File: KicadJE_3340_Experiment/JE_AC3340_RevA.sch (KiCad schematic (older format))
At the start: 64 parts

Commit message: Update JE_AC3340_RevA.sch
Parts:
- added C?: 10n, Capacitor_SMD:C_0805_2012Metric_Pad1.15x1.40mm_HandSolder, symbol Device:C
- added C?: 1n alt, Capacitor_SMD:C_0805_2012Metric_Pad1.15x1.40mm_HandSolder, symbol Device:C
- added C?: 1n poly, Capacitor_THT:C_Rect_L7.0mm_W2.0mm_P5.00mm, symbol Device:C
- added C? (x2): 100n, Capacitor_SMD:C_0805_2012Metric_Pad1.15x1.40mm_HandSolder, symbol Device:C
- added C?: 220p, Capacitor_SMD:C_0805_2012Metric_Pad1.15x1.40mm_HandSolder, symbol Device:C
- added D?: 1N4148, Diode_SMD:D_SOD-123, symbol Device:D
- added D?: Germanium, symbol Device:D
- added JP?: Jumper_3_Bridged12, Jumper:SolderJumper-3_P1.3mm_Bridged12_Pad1.0x1.5mm_NumberLabels, symbol Jumper:Jumper_3_Bridged12
- added Q?: MMBT3906, Package_TO_SOT_SMD:SOT-23, symbol Transistor_BJT:MMBT3906
- added R? (x4): 100k, Resistor_SMD:R_0805_2012Metric_Pad1.15x1.40mm_HandSolder, symbol Device:R
- added R?: 10k, Resistor_SMD:R_0805_2012Metric_Pad1.15x1.40mm_HandSolder, symbol Device:R
- added R?: 20k, Resistor_SMD:R_0805_2012Metric_Pad1.15x1.40mm_HandSolder, symbol Device:R
- added R?: 1k82, Resistor_SMD:R_0805_2012Metric_Pad1.15x1.40mm_HandSolder, symbol Device:R
- added R?: 6k04, Resistor_SMD:R_0805_2012Metric_Pad1.15x1.40mm_HandSolder, symbol Device:R
- added R?: 26k7, Resistor_SMD:R_0805_2012Metric_Pad1.15x1.40mm_HandSolder, symbol Device:R
- added R?: 1M2, Resistor_SMD:R_0805_2012Metric_Pad1.15x1.40mm_HandSolder, symbol Device:R
- added R? (x2): 47k, Resistor_SMD:R_0805_2012Metric_Pad1.15x1.40mm_HandSolder, symbol Device:R
- added RV?: 5k, Potentiometer_THT:Potentiometer_Bourns_3296W_Vertical, symbol Device:R_POT_TRIM
- added U?: TL072, AJ-Dropbox-Kicad:AJ_SO-8_5.3x6.2mm_P1.27mm, symbol Amplifier_Operational:TL072
- added U?: AS3340, symbol Audio:AS3340
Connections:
- net +12L: no longer U?.16 (VCC)
- net +12VA: now also U?.16 (VCC), U?.16 (VCC)
- net +5V: now also JP?.1 (A)
- net -12VA: now also R?.2
- net -5V: now also R?.2, R?.2, RV?.1, RV?.2, U?.3 (VEE)
- net CVIn1: now also U?.15 (VFCI)
- net FM_Lin_In4: now also U?.13 (VLFI)
- net GND: now also C?.1, C?.1, C?.1, C?.2, R?.1, R?.1, U?.12 (GND), U?.3 (+), U?.7 (VHFT)
- net PWM_In5: now also C?.2, D?.1 (K), R?.1, U?.1, U?.5 (VPWM); no longer D?.1 (K), D?.2 (A), R?.1
- net SoftSyncIn2: now also C?.2
- net VP_2: now also R?.2, U?.4 (VP)
- net VSO_3: now also Q?.2 (E), U?.8 (VSO)
- net VTO_1: now also U?.10 (VTO)
- net Vee: no longer R?.2, RV?.1, RV?.2
- new net: D?.1 (K), D?.2 (A), R?.1, R?.2
- new net: R?.2, RV?.1, RV?.2
- new net: C?.1, D?.2 (A), R?.1, R?.1, R?.1, R?.2, U?.2 (-)
- new net: R?.1, R?.2
- new net: R?.1, U?.1 (SCALE1)
- new net: C?.1, C?.2, U?.11 (CAP)
- new net: R?.2, U?.14 (VS)
- new net: R?.1, R?.1, U?.2 (SCALE2)
- new net: C?.2, JP?.3 (B), U?.9 (VSSI)
- new net: R?.2, RV?.3
- new net: D?.1 (K), Q?.1 (B), R?.1, R?.1
- new net: C?.2, D?.2 (A), Q?.3 (C)
- new net: C?.1, R?.2
- new net: JP?.2 (C), R?.2
- new net poly: R?.2
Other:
- note added: "1n timing cap\n0805 as backup\nTHT 1000 pf poly"
- note added: "Prophet 5"
- note added: "Prophet T8"

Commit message: Octave switch JE
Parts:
- added R?: 82k, Resistor_SMD:R_0805_2012Metric_Pad1.15x1.40mm_HandSolder, symbol Device:R
- added R?: 20k, Resistor_SMD:R_0805_2012Metric_Pad1.15x1.40mm_HandSolder, symbol Device:R
- added R?: 47k, Resistor_SMD:R_0805_2012Metric_Pad1.15x1.40mm_HandSolder, symbol Device:R
- added R?: 470R, Resistor_SMD:R_0805_2012Metric_Pad1.15x1.40mm_HandSolder, symbol Device:R
- added SW?: Octave (3 state), AJ-Dropbox-Kicad:SP1MS1, symbol Switch:SW_SPDT
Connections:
- net +5V: now also R?.2, R?.2
- net GND: now also R?.2, SW?.1 (A)
- new net: R?.1, R?.2, SW?.2 (B)
- new net: R?.1, SW?.3 (C)
- new net: R?.1, R?.1
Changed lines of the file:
@@
 AR Path="/5E4B0DD9/5F66CD2B" Ref="U?"  Part="1"
 AR Path="/5E62ACA1/5F66CD2B" Ref="U?"  Part="1"
+AR Path="/5F49A670/5F66CD2B" Ref="U?"  Part="1"
 F 0 "U?" H 10300 4631 50  0000 C CNN
 F 1 "AS3340" H 10300 4540 50  0000 C CNN
@@
 AR Path="/5E4B0DD9/5F66CD3F" Ref="C?"  Part="1"
 AR Path="/5E62ACA1/5F66CD3F" Ref="C?"  Part="1"
+AR Path="/5F49A670/5F66CD3F" Ref="C?"  Part="1"
 F 0 "C?" H 9200 4450 50  0000 L CNN
 F 1 "1n poly" H 9125 4200 50  0000 L CNN
@@
 AR Path="/5E4B0DD9/5F66CD4A" Ref="R?"  Part="1"
 AR Path="/5E62ACA1/5F66CD4A" Ref="R?"  Part="1"
+AR Path="/5F49A670/5F66CD4A" Ref="R?"  Part="1"
 F 0 "R?" V 9550 4450 50  0000 C CNN
 F 1 "1k82" V 9675 4450 50  0000 C CNN
@@
 AR Path="/5E4B0DD9/5F66CD58" Ref="#PWR?"  Part="1"
 AR Path="/5E62ACA1/5F66CD58" Ref="#PWR?"  Part="1"
+AR Path="/5F49A670/5F66CD58" Ref="#PWR?"  Part="1"
 F 0 "#PWR?" H 9425 4400 50  0001 C CNN
 F 1 "GND" H 9430 4477 50  0000 C CNN
@@
 AR Path="/5E4B0DD9/5F66CD63" Ref="R?"  Part="1"
 AR Path="/5E62ACA1/5F66CD63" Ref="R?"  Part="1"
+AR Path="/5F49A670/5F66CD63" Ref="R?"  Part="1"
 F 0 "R?" V 9375 3400 50  0000 C CNN
 F 1 "6k04" V 9425 3250 50  0000 C CNN
@@
 AR Path="/5E4B0DD9/5F66CD69" Ref="R?"  Part="1"
 AR Path="/5E62ACA1/5F66CD69" Ref="R?"  Part="1"
+AR Path="/5F49A670/5F66CD69" Ref="R?"  Part="1"
 F 0 "R?" V 9325 3275 50  0000 C CNN
 F 1 "26k7" V 9425 3150 50  0000 C CNN
@@
 AR Path="/5E4B0DD9/5F66CD6F" Ref="RV?"  Part="1"
 AR Path="/5E62ACA1/5F66CD6F" Ref="RV?"  Part="1"
+AR Path="/5F49A670/5F66CD6F" Ref="RV?"  Part="1"
 F 0 "RV?" V 9150 3050 50  0000 C CNN
 F 1 "5k" V 9025 3175 50  0000 C CNN
@@
 AR Path="/5E4B0DD9/5F66CD7D" Ref="#PWR?"  Part="1"
 AR Path="/5E62ACA1/5F66CD7D" Ref="#PWR?"  Part="1"
+AR Path="/5F49A670/5F66CD7D" Ref="#PWR?"  Part="1"
 F 0 "#PWR?" H 10400 4350 50  0001 C CNN
 F 1 "GND" H 10405 4427 50  0000 C CNN
@@
 AR Path="/5E4B0DD9/5F66CD91" Ref="R?"  Part="1"
 AR Path="/5E62ACA1/5F66CD91" Ref="R?"  Part="1"
+AR Path="/5F49A670/5F66CD91" Ref="R?"  Part="1"
 F 0 "R?" V 9375 3500 50  0000 C CNN
 F 1 "1M2" V 9425 3350 50  0000 C CNN
@@
 U 1 1 5F66CD99
 P 8675 3150
+AR Path="/5E62ACA1/5F66CD99" Ref="#PWR?"  Part="1"
+AR Path="/5F49A670/5F66CD99" Ref="#PWR?"  Part="1"
 F 0 "#PWR?" H 8675 3250 50  0001 C CNN
 F 1 "-5V" H 8690 3323 50  0000 C CNN
@@
 AR Path="/5E4B0DD9/5F66CD9F" Ref="#PWR?"  Part="1"
 AR Path="/5E62ACA1/5F66CD9F" Ref="#PWR?"  Part="1"
+AR Path="/5F49A670/5F66CD9F" Ref="#PWR?"  Part="1"
 F 0 "#PWR?" H 9125 3225 50  0001 C CNN
 F 1 "-12VA" H 9140 3548 50  0000 C CNN
@@
 AR Path="/5F18E4B5/5F66CDA9" Ref="C?"  Part="1"
 AR Path="/5E62ACA1/5F66CDA9" Ref="C?"  Part="1"
+AR Path="/5F49A670/5F66CDA9" Ref="C?"  Part="1"
 F 0 "C?" H 8925 4450 50  0000 L CNN
 F 1 "100n" H 8850 4275 50  0000 L CNN
@@
 U 1 1 5F66CDB6
 P 10300 4625
+AR Path="/5E62ACA1/5F66CDB6" Ref="#PWR?"  Part="1"
+AR Path="/5F49A670/5F66CDB6" Ref="#PWR?"  Part="1"
 F 0 "#PWR?" H 10300 4725 50  0001 C CNN
 F 1 "-5V" H 10315 4798 50  0000 C CNN
@@
 U 1 1 5F66CDBC
 P 8550 3950
+AR Path="/5E62ACA1/5F66CDBC" Ref="Q?"  Part="1"
+AR Path="/5F49A670/5F66CDBC" Ref="Q?"  Part="1"
 F 0 "Q?" H 8741 3904 50  0000 L CNN
 F 1 "MMBT3906" H 8741 3995 50  0000 L CNN
@@
 AR Path="/5E4B0DD9/5F66CDC3" Ref="C?"  Part="1"
 AR Path="/5E62ACA1/5F66CDC3" Ref="C?"  Part="1"
+AR Path="/5F49A670/5F66CDC3" Ref="C?"  Part="1"
 F 0 "C?" V 7550 4150 50  0000 L CNN
 F 1 "220p" V 7650 4150 50  0000 L CNN
@@
 AR Path="/5E4B0DD9/5F66CDC9" Ref="R?"  Part="1"
 AR Path="/5E62ACA1/5F66CDC9" Ref="R?"  Part="1"
+AR Path="/5F49A670/5F66CDC9" Ref="R?"  Part="1"
 F 0 "R?" V 7900 4025 50  0000 C CNN
 F 1 "47k" V 8000 4100 50  0000 C CNN
@@
 AR Path="/5E4B0DD9/5F66CDD1" Ref="R?"  Part="1"
 AR Path="/5E62ACA1/5F66CDD1" Ref="R?"  Part="1"
+AR Path="/5F49A670/5F66CDD1" Ref="R?"  Part="1"
 F 0 "R?" V 8125 3725 50  0000 C CNN
 F 1 "47k" V 8225 3800 50  0000 C CNN
@@
 U 1 1 5F66CDDA
 P 7975 3400
+AR Path="/5E62ACA1/5F66CDDA" Ref="#PWR?"  Part="1"
+AR Path="/5F49A670/5F66CDDA" Ref="#PWR?"  Part="1"
 F 0 "#PWR?" H 7975 3250 50  0001 C CNN
 F 1 "+5V" H 7990 3573 50  0000 C CNN
@@
 AR Path="/5F18E4B5/5F66CDE3" Ref="C?"  Part="1"
 AR Path="/5E62ACA1/5F66CDE3" Ref="C?"  Part="1"
+AR Path="/5F49A670/5F66CDE3" Ref="C?"  Part="1"
 F 0 "C?" H 8650 4450 50  0000 L CNN
 F 1 "100n" H 8550 4275 50  0000 L CNN
@@
 U 1 1 5F66CDEE
 P 8425 4175
+AR Path="/5E62ACA1/5F66CDEE" Ref="D?"  Part="1"
+AR Path="/5F49A670/5F66CDEE" Ref="D?"  Part="1"
 F 0 "D?" H 8325 4250 50  0000 C CNN
 F 1 "Germanium" H 8325 4100 50  0000 C CNN
@@
 U 1 1 5F66CDFA
 P 8225 3450
+AR Path="/5E62ACA1/5F66CDFA" Ref="JP?"  Part="1"
+AR Path="/5F49A670/5F66CDFA" Ref="JP?"  Part="1"
 F 0 "JP?" H 8225 3654 50  0000 C CNN
 F 1 "Jumper_3_Bridged12" H 8225 3563 50  0000 C CNN
@@
 	1    0    0    -1
 $EndComp
+$Comp
+L Switch:SW_SPDT SW?
+U 1 1 5F6B865F
+P 1700 5675
+AR Path="/5F6B865F" Ref="SW?"  Part="1"
+AR Path="/5C8C5FC0/5F6B865F" Ref="SW?"  Part="1"
+AR Path="/5CAAE8D3/5F6B865F" Ref="SW?"  Part="1"
+AR Path="/5E4B0DD9/5F6B865F" Ref="SW?"  Part="1"
+AR Path="/5E62ACA1/5F6B865F" Ref="SW?"  Part="1"
+AR Path="/5F49A670/5F6B865F" Ref="SW?"  Part="1"
+F 0 "SW?" H 2100 5700 50  0000 C CNN
+F 1 "Octave (3 state)" H 1750 5475 50  0000 C CNN
+F 2 "AJ-Dropbox-Kicad:SP1MS1" H 1700 5675 50  0001 C CNN
+F 3 "~" H 1700 5675 50  0001 C CNN
+	1    1700 5675
+	-1   0    0    1
+$EndComp
+$Comp
+L Envelope-cache-2018-08-04-13-00-04:+5V #PWR?
+U 1 1 5F6F74CC
+P 1500 5300
+AR Path="/5E62ACA1/5F6F74CC" Ref="#PWR?"  Part="1"
+AR Path="/5F49A670/5F6F74CC" Ref="#PWR?"  Part="1"
+F 0 "#PWR?" H 1500 5150 50  0001 C CNN
+F 1 "+5V" H 1515 5473 50  0000 C CNN
+F 2 "" H 1500 5300 50  0001 C CNN
+F 3 "" H 1500 5300 50  0001 C CNN
+	1    1500 5300
+	1    0    0    -1
+$EndComp
+$Comp
+L Device:R R?
+U 1 1 5F6F7A40
+P 2025 5500
+AR Path="/5F6F7A40" Ref="R?"  Part="1"
+AR Path="/5C8C5FC0/5F6F7A40" Ref="R?"  Part="1"
+AR Path="/5CAAE8D3/5F6F7A40" Ref="R?"  Part="1"
+AR Path="/5E4B0DD9/5F6F7A40" Ref="R?"  Part="1"
+AR Path="/5E62ACA1/5F6F7A40" Ref="R?"  Part="1"
+AR Path="/5F49A670/5F6F7A40" Ref="R?"  Part="1"
+F 0 "R?" V 1950 5425 50  0000 C CNN
+F 1 "82k" V 2025 5500 50  0000 C CNN
+F 2 "Resistor_SMD:R_0805_2012Metric_Pad1.15x1.40mm_HandSolder" V 1955 5500 50  0001 C CNN
+F 3 "~" H 2025 5500 50  0001 C CNN
+	1    2025 5500
+	-1   0    0    1
+$EndComp
+$Comp
+L Device:R R?
+U 1 1 5F6F8705
+P 2025 5850
+AR Path="/5F6F8705" Ref="R?"  Part="1"
+AR Path="/5C8C5FC0/5F6F8705" Ref="R?"  Part="1"
+AR Path="/5CAAE8D3/5F6F8705" Ref="R?"  Part="1"
+AR Path="/5E4B0DD9/5F6F8705" Ref="R?"  Part="1"
+AR Path="/5E62ACA1/5F6F8705" Ref="R?"  Part="1"
+AR Path="/5F49A670/5F6F8705" Ref="R?"  Part="1"
+F 0 "R?" V 1950 5775 50  0000 C CNN
+F 1 "20k" V 2025 5850 50  0000 C CNN
+F 2 "Resistor_SMD:R_0805_2012Metric_Pad1.15x1.40mm_HandSolder" V 1955 5850 50  0001 C CNN
+F 3 "~" H 2025 5850 50  0001 C CNN
+	1    2025 5850
+	-1   0    0    1
+$EndComp
+$Comp
+L Envelope-cache-2018-08-04-13-00-04:GND #PWR?
+U 1 1 5F6F8CBF
+P 1500 6050
+AR Path="/5F6F8CBF" Ref="#PWR?"  Part="1"
+AR Path="/5C8C5FC0/5F6F8CBF" Ref="#PWR?"  Part="1"
+AR Path="/5CAAE8D3/5F6F8CBF" Ref="#PWR?"  Part="1"
+AR Path="/5E4B0DD9/5F6F8CBF" Ref="#PWR?"  Part="1"
+AR Path="/5F49A670/5F6F8CBF" Ref="#PWR?"  Part="1"
+F 0 "#PWR?" H 1500 5800 50  0001 C CNN
+F 1 "GND" H 1505 5877 50  0000 C CNN
+F 2 "" H 1500 6050 50  0001 C CNN
+F 3 "" H 1500 6050 50  0001 C CNN
+	1    1500 6050
+	1    0    0    -1
+$EndComp
+Wire Wire Line
+	2025 5350 2025 5325
+Wire Wire Line
+	2025 5325 1500 5325
+Wire Wire Line
+	1500 5325 1500 5300
+Wire Wire Line
+	1500 6050 1500 6025
+Wire Wire Line
+	1500 6025 1625 6025
+Wire Wire Line
+	2025 6025 2025 6000
+Wire Wire Line
+	2025 5700 2025 5675
+Wire Wire Line
+	1900 5675 2025 5675
+Connection ~ 2025 5675
+Wire Wire Line
+	2025 5675 2025 5650
+$Comp
+L Device:R R?
+U 1 1 5F753A2A
+P 1250 5475
+AR Path="/5F753A2A" Ref="R?"  Part="1"
+AR Path="/5C8C5FC0/5F753A2A" Ref="R?"  Part="1"
+AR Path="/5CAAE8D3/5F753A2A" Ref="R?"  Part="1"
+AR Path="/5E4B0DD9/5F753A2A" Ref="R?"  Part="1"
+AR Path="/5E62ACA1/5F753A2A" Ref="R?"  Part="1"
+AR Path="/5F49A670/5F753A2A" Ref="R?"  Part="1"
+F 0 "R?" V 1175 5400 50  0000 C CNN
+F 1 "47k" V 1250 5475 50  0000 C CNN
+F 2 "Resistor_SMD:R_0805_2012Metric_Pad1.15x1.40mm_HandSolder" V 1180 5475 50  0001 C CNN
+F 3 "~" H 1250 5475 50  0001 C CNN
+	1    1250 5475
+	-1   0    0    1
+$EndComp
+Wire Wire Line
+	1250 5325 1500 5325
+Connection ~ 1500 5325
+Wire Wire Line
+	1250 5625 1500 5625
+Wire Wire Line
+	1500 5625 1500 5575
+Wire Wire Line
+	1500 5775 1500 6025
+Connection ~ 1500 6025
+$Comp
+L Device:R R?
+U 1 1 5F79A77D
+P 1775 6025
+AR Path="/5F79A77D" Ref="R?"  Part="1"
+AR Path="/5C8C5FC0/5F79A77D" Ref="R?"  Part="1"
+AR Path="/5CAAE8D3/5F79A77D" Ref="R?"  Part="1"
+AR Path="/5E4B0DD9/5F79A77D" Ref="R?"  Part="1"
+AR Path="/5F49A670/5F79A77D" Ref="R?"  Part="1"
+F 0 "R?" V 1650 6025 50  0000 C CNN
+F 1 "470R" V 1775 6025 50  0000 C CNN
+F 2 "Resistor_SMD:R_0805_2012Metric_Pad1.15x1.40mm_HandSolder" V 1705 6025 50  0001 C CNN
+F 3 "~" H 1775 6025 50  0001 C CNN
+	1    1775 6025
+	0    1    1    0
+$EndComp
+Wire Wire Line
+	1925 6025 2025 6025
 $EndSCHEMATC

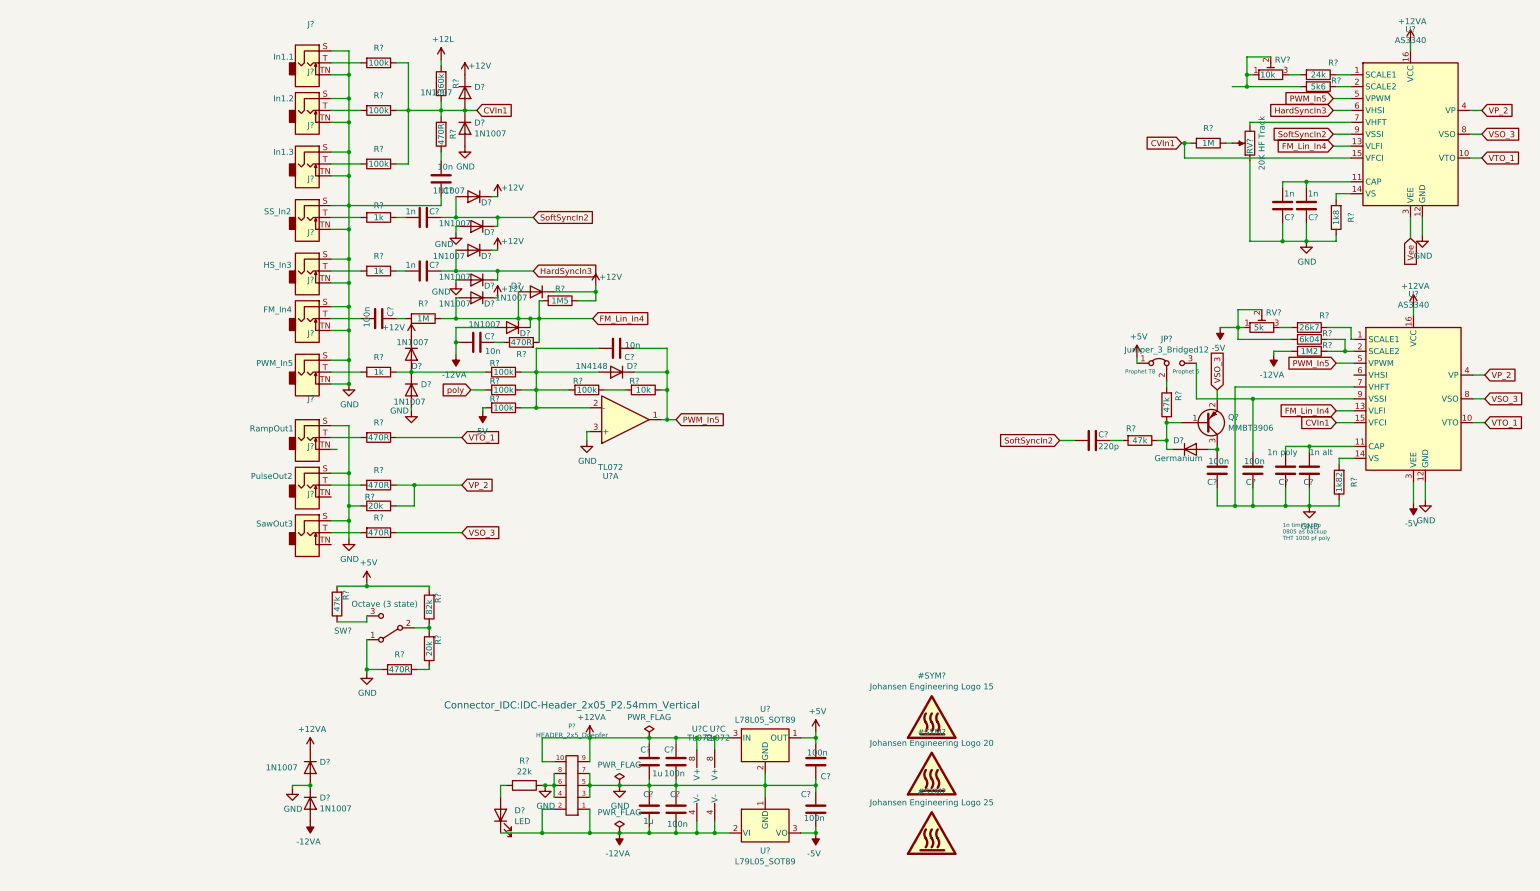
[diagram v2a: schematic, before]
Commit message: cleaning up and migrating data sheet features
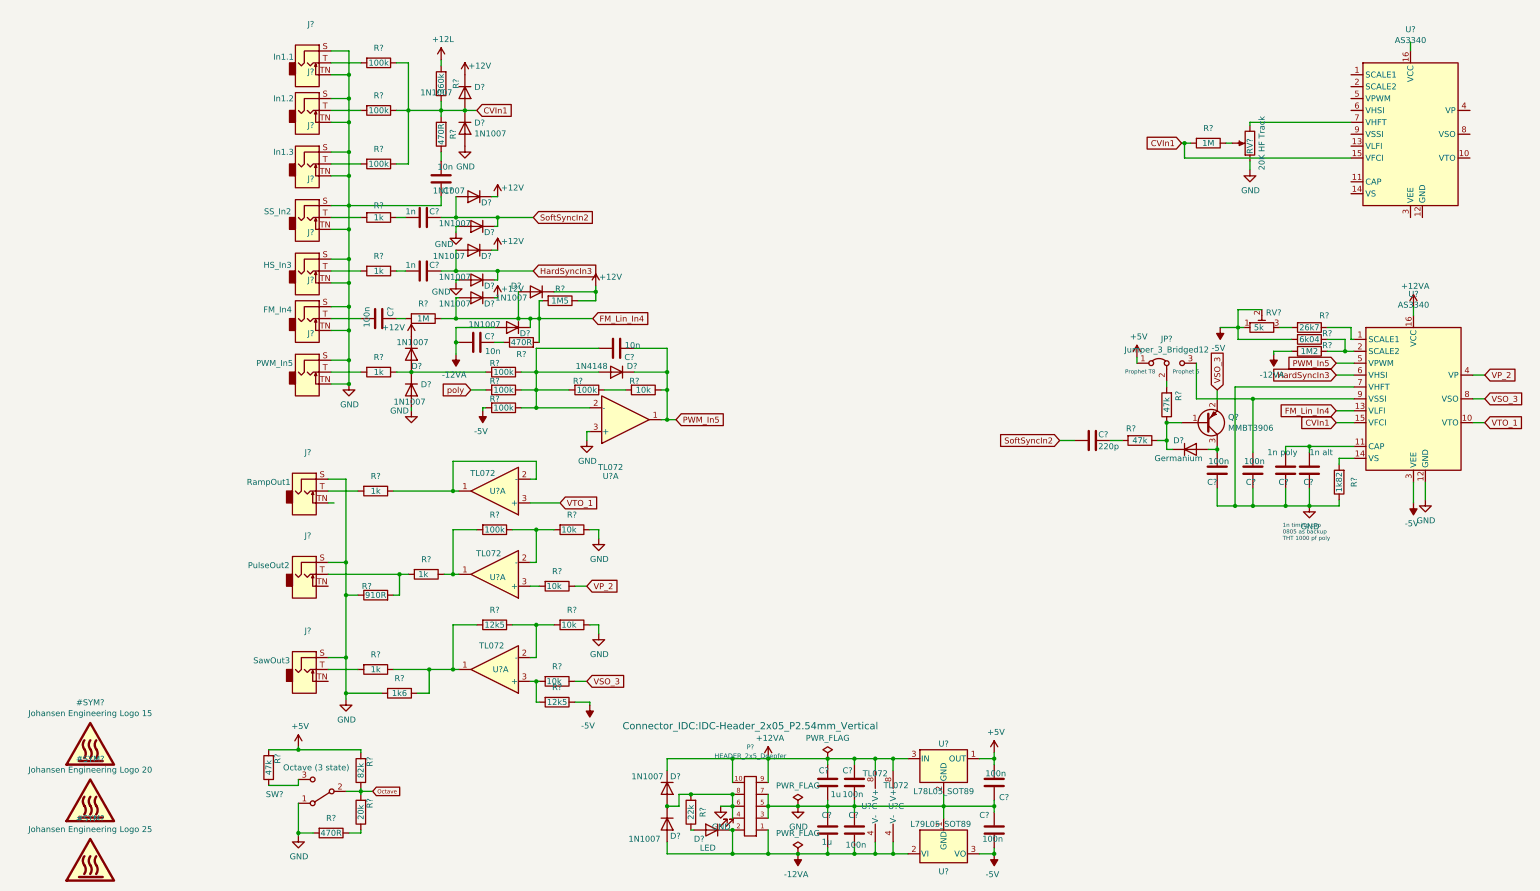
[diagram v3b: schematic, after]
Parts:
- removed C? (x2): 1n, Capacitor_SMD:C_0805_2012Metric_Pad1.15x1.40mm_HandSolder, symbol Device:C
- removed R?: 1k8, Resistor_SMD:R_0805_2012Metric_Pad1.15x1.40mm_HandSolder, symbol Device:R
- removed R?: 5k6, Resistor_SMD:R_0805_2012Metric_Pad1.15x1.40mm_HandSolder, symbol Device:R
- removed R?: 24k, Resistor_SMD:R_0805_2012Metric_Pad1.15x1.40mm_HandSolder, symbol Device:R
- removed RV?: 10k, symbol Device:R_POT_TRIM
- added R?: 1k6, Resistor_SMD:R_0805_2012Metric_Pad1.15x1.40mm_HandSolder, symbol Device:R
- added R?: 100k, Resistor_SMD:R_0805_2012Metric_Pad1.15x1.40mm_HandSolder, symbol Device:R
- added R? (x4): 10k, Resistor_SMD:R_0805_2012Metric_Pad1.15x1.40mm_HandSolder, symbol Device:R
- added R? (x2): 12k5, Resistor_SMD:R_0805_2012Metric_Pad1.15x1.40mm_HandSolder, symbol Device:R
- added U? (x3): TL072, AJ-Dropbox-Kicad:AJ_SO-8_5.3x6.2mm_P1.27mm, symbol Amplifier_Operational:TL072
- R? (x3): value 470R -> 1k
- R?: value 20k -> 910R
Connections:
- net +12VA: no longer U?.16 (VCC)
- net -5V: now also R?.1
- net FM_Lin_In4: no longer U?.13 (VLFI)
- net GND: now also R?.2, R?.1, R?.1, R?.2; no longer R?.1, U?.12 (GND)
- net HardSyncIn3: now also U?.6 (VHSI); no longer U?.6 (VHSI)
- net PWM_In5: no longer U?.5 (VPWM)
- net SoftSyncIn2: no longer U?.9 (VSSI)
- net VP_2: now also R?.1; no longer R?.1, R?.2, U?.4 (VP)
- net VSO_3: now also R?.1; no longer R?.1, U?.8 (VSO)
- net VTO_1: now also U?.3 (+); no longer R?.1, U?.10 (VTO)
- net at J?.T, R?.2: now also R?.2
- net at D?.2 (A): now also R?.1; no longer R?.2
- net Octave: now reaches R?.1, R?.2, SW?.2 (B)
- net Vee: no longer names the net of U?.3 (VEE)
- new net: R?.1, R?.1, R?.2, U?.1
- new net: R?.1, R?.2, U?.1
- new net: R?.1, U?.1, U?.2 (-)
- new net: R?.1, R?.2, U?.2 (-) (x2)
- new net: R?.2, U?.3 (+)
- new net: R?.2, R?.2, U?.3 (+)
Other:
- moved on the sheet: C?, D?, J?, P?, R?, SW?, U?, U?C
